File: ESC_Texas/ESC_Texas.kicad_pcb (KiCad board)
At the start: 4 copper layers, 118 x 72 mm, 149 parts, among them IC1 nRF52840-QFAA-F-R7, IC10 UCC21331CQDRQ1, IC11 LM3480IM3-3.3_NOPB, IC2 UCC21331CQDRQ1, IC3 AD8411AWBRZ, IC4 MC78L05ACHT1G, IC5 AD8411AWBRZ, IC6 MC78L05ACHT1G, IC7 UCC21331CQDRQ1, IC8 AD8411AWBRZ, IC9 MC78L05ACHT1G, J1 Conn_01x10_Pin, J10 Conn_01x03_Pin, J12 Conn_01x05_Pin, J13 Conn_01x06_Pin, J2 Conn_01x05_Pin, J3 Motor, J4 Conn_01x05_Pin, J5 Conn_01x03_Pin, J6 Conn_01x03_Pin, J7 Conn_01x03_Pin, J8 Conn_01x03_Pin, J9 Conn_01x03_Pin, Q1 IPD100N06S4, Q2 IPD100N06S4, Q3 IPD100N06S4, Q4 IPD100N06S4, Q5 IPD100N06S4, Q6 IPD100N06S4, Y1 CM7V-T1A-32.768kHz, Y2 32MHz

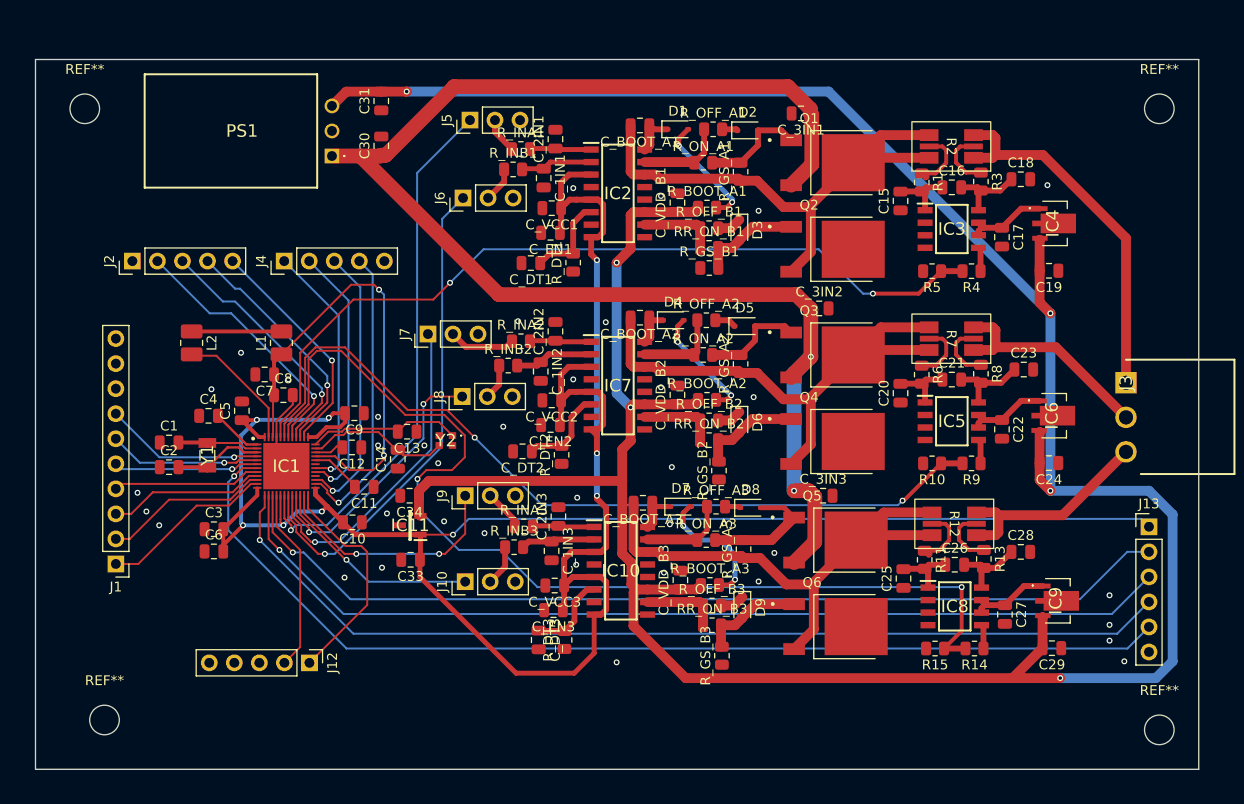
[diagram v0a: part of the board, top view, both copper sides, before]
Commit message: Removed excess pin headers
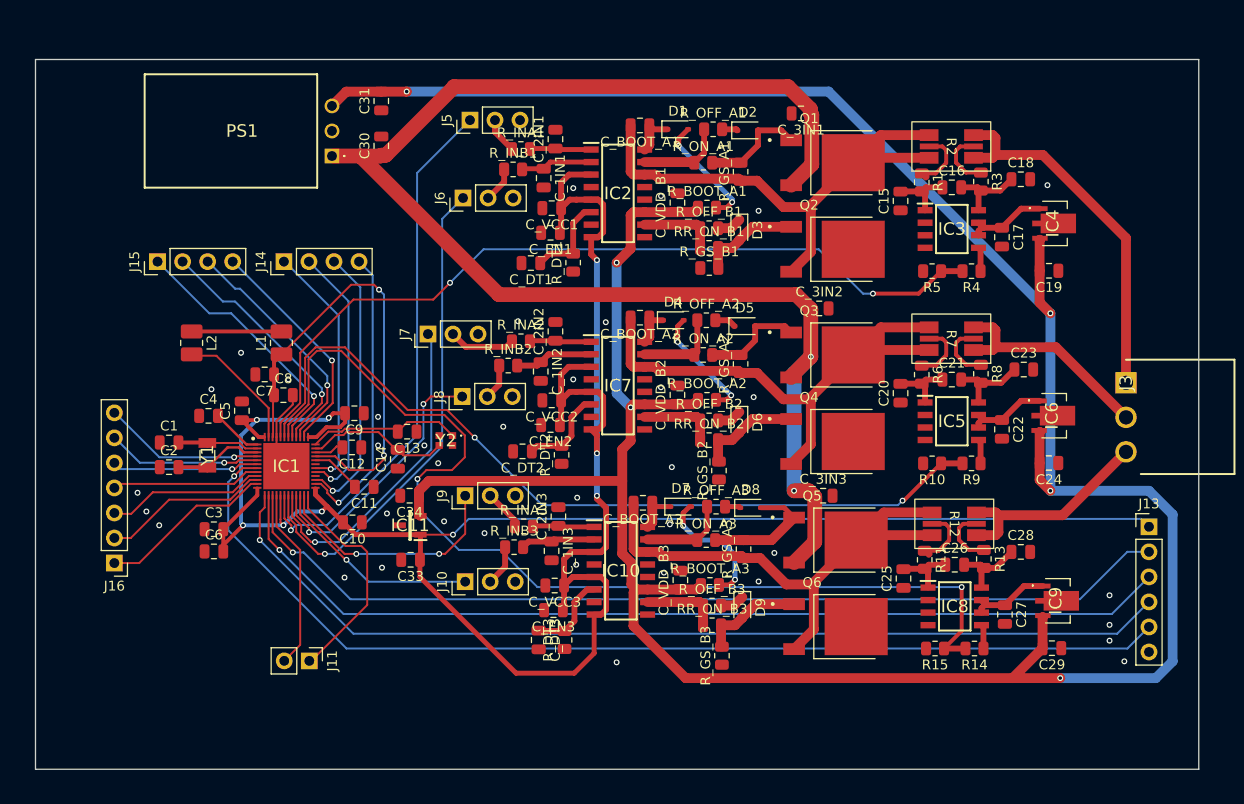
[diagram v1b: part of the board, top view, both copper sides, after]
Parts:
- removed J1: Conn_01x10_Pin, Connector_PinHeader_2.54mm:PinHeader_1x10_P2.54mm_Vertical
- removed J12, J2, J4: Conn_01x05_Pin, Connector_PinHeader_2.54mm:PinHeader_1x05_P2.54mm_Vertical
- removed REF** (x4): MountingHole_3mm, MountingHole:MountingHole_3mm
- added J11: Conn_01x02_Pin, Connector_PinHeader_2.54mm:PinHeader_1x02_P2.54mm_Vertical, F.Cu at (119.8, 135.0)
- added J14: Conn_01x04_Pin, Connector_PinHeader_2.54mm:PinHeader_1x04_P2.54mm_Vertical, F.Cu at (117.2, 94.5)
- added J15: Conn_01x04_Pin, Connector_PinHeader_2.54mm:PinHeader_1x04_P2.54mm_Vertical, F.Cu at (104.4, 94.5)
- added J16: Conn_01x07_Pin, Connector_PinHeader_2.54mm:PinHeader_1x07_P2.54mm_Vertical, F.Cu at (100.0, 125.1)
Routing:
- net P0.03: track 24.8 -> 24.3 mm

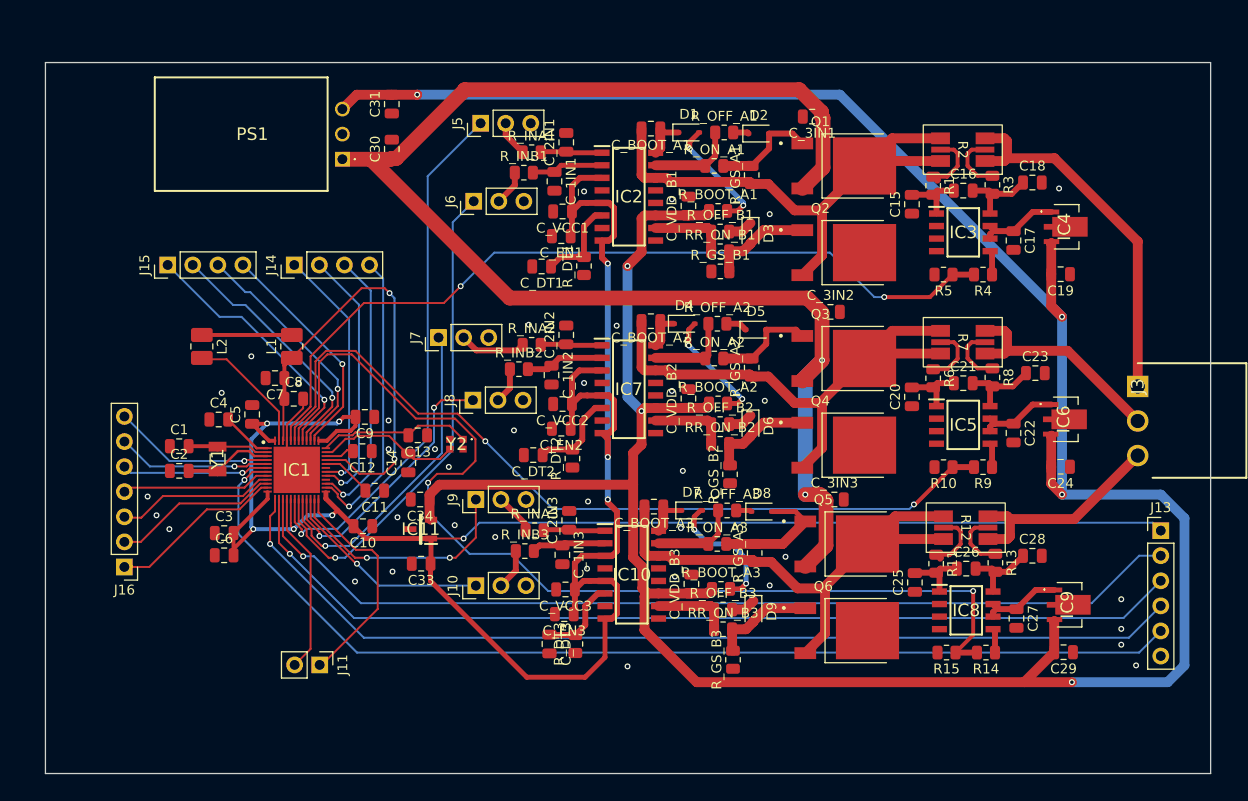
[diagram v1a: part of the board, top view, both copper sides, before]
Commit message: More gnd vias added
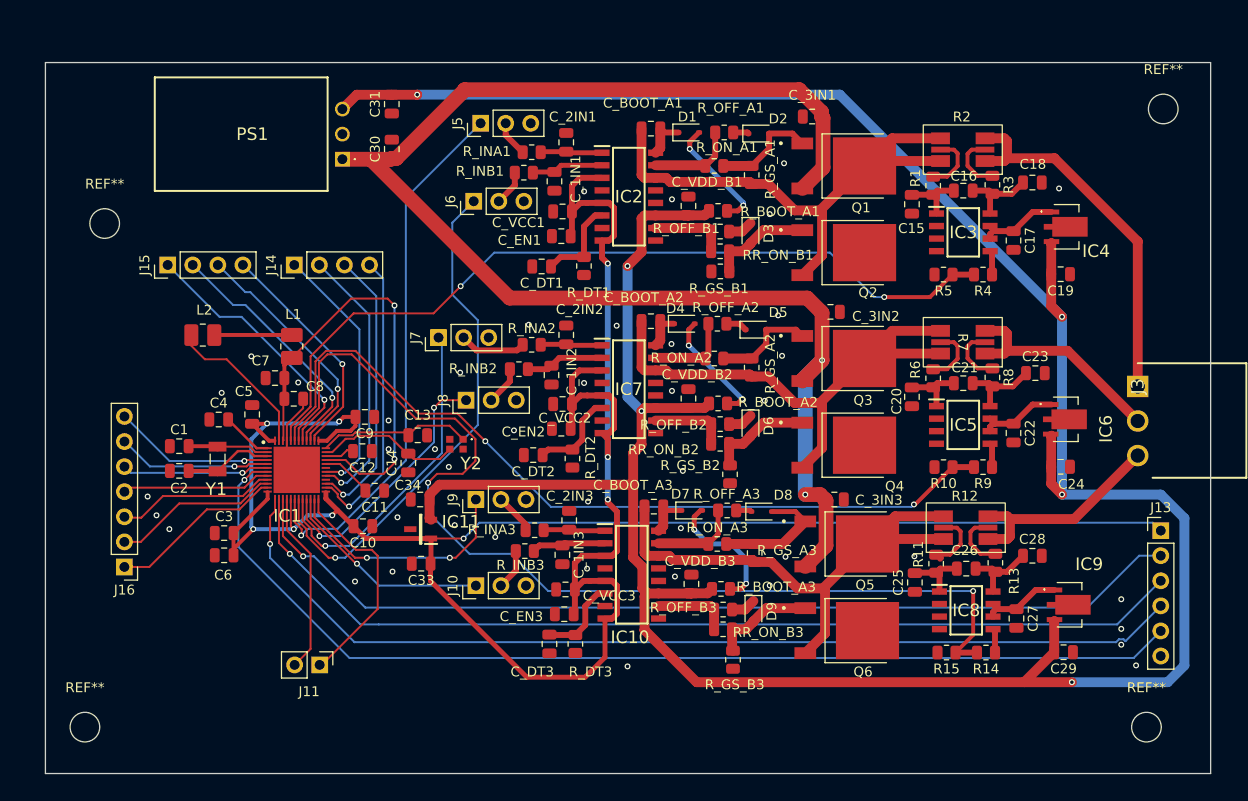
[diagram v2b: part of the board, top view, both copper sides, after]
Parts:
- added REF**: MountingHole_3mm, MountingHole:MountingHole_3mm, F.Cu at (98.0, 90.3)
- added REF**: MountingHole_3mm, MountingHole:MountingHole_3mm, F.Cu at (203.5, 141.3)
- added REF**: MountingHole_3mm, MountingHole:MountingHole_3mm, F.Cu at (205.2, 78.7)
- added REF**: MountingHole_3mm, MountingHole:MountingHole_3mm, F.Cu at (96.0, 141.3)
- moved L2 1.15 mm to (107.9, 101.6), turned to 180 degrees
- moved J8 0.69 mm to (134.6, 108.2)
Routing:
- net Net-(IC1-DCC): track 13.0 -> 15.7 mm
- net P0.20: track 50.4 -> 52.5 mm
- net P0.13: track 100.2 -> 101.6 mm
- net DEC6: track 47.2 -> 45.9 mm
- net Net-(L1-Pad2): track 9.11 -> 7.86 mm
- net P0.08: track 107.7 -> 108.9 mm
- net P0.09: track 26.7 -> 27.6 mm
- net P0.10: track 25.6 -> 26.4 mm
- net P0.22: track 27.6 -> 26.9 mm
- net GND: vias 37 -> 43

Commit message: Started new additions
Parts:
- removed REF** (x4): MountingHole_3mm, MountingHole:MountingHole_3mm
- moved C15 2.34 mm to (180.2, 90.7)
- moved Q2 1.60 mm to (171.3, 93.2)
- moved Q1 1.53 mm to (171.6, 83.6)
- moved C_3IN2 0.65 mm to (170.8, 99.2), turned to 180 degrees
- moved C_3IN1 0.65 mm to (169.2, 79.0)
- moved Q5 0.14 mm to (173.3, 122.8)
- moved Q3 0.11 mm to (172.8, 104.0)
- moved Q6 0.10 mm to (173.2, 131.6)
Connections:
- Q1 pad 2: /Phase1/Driver_subsheet_1/VSSA -> +36V
- Q1 pad 3: +36V -> /Phase1/Driver_subsheet_1/VSSA
- Q2 pad 2: GND -> /Phase1/Driver_subsheet_1/VSSA
- Q2 pad 3: /Phase1/Driver_subsheet_1/VSSA -> GND
- Q3 pad 2: /Phase2/Driver_subsheet_1/VSSA -> +36V
- Q3 pad 3: +36V -> /Phase2/Driver_subsheet_1/VSSA
- Q4 pad 2: GND -> /Phase2/Driver_subsheet_1/VSSA
- Q4 pad 3: /Phase2/Driver_subsheet_1/VSSA -> GND
- Q5 pad 2: /Phase3/Driver_subsheet_1/VSSA -> +36V
- Q5 pad 3: +36V -> /Phase3/Driver_subsheet_1/VSSA
- Q6 pad 2: GND -> /Phase3/Driver_subsheet_1/VSSA
- Q6 pad 3: /Phase3/Driver_subsheet_1/VSSA -> GND
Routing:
- net +36V: track 145.1 -> 63.4 mm, vias 2 -> 27
- net /Phase3/Driver_subsheet_1/VSSA: track 55.0 -> 18.5 mm
- net /Phase2/Driver_subsheet_1/VSSA: track 55.0 -> 32.2 mm
- net /Phase1/Driver_subsheet_1/VSSA: track 55.0 -> 38.7 mm
- net /Phase3/Driver_subsheet_1/GateA: track 12.7 -> 8.08 mm
- net /Phase2/Driver_subsheet_1/GateB: track 10.5 -> 6.62 mm
- net /Phase2/Driver_subsheet_1/GateA: track 10.3 -> 6.41 mm
- net /Phase3/Driver_subsheet_1/GateB: track 10.5 -> 7.16 mm
- net Net-(IC3--IN): track 6.48 -> 4.32 mm
- net /Phase1/Driver_subsheet_1/GateB: track 10.4 -> 8.74 mm
- net /Phase1/Driver_subsheet_1/GateA: track 10.7 -> 9.05 mm
- net P0.31: track 83.7 -> 84.6 mm
- net GND: vias 43 -> 44
- added copper zone on B.Cu, net +36V
- added copper zone on F.Cu, net +36V
- added copper zone on In2.Cu, net +36V
- added copper zone on F.Cu, net /Phase1/Driver_subsheet_1/VSSA

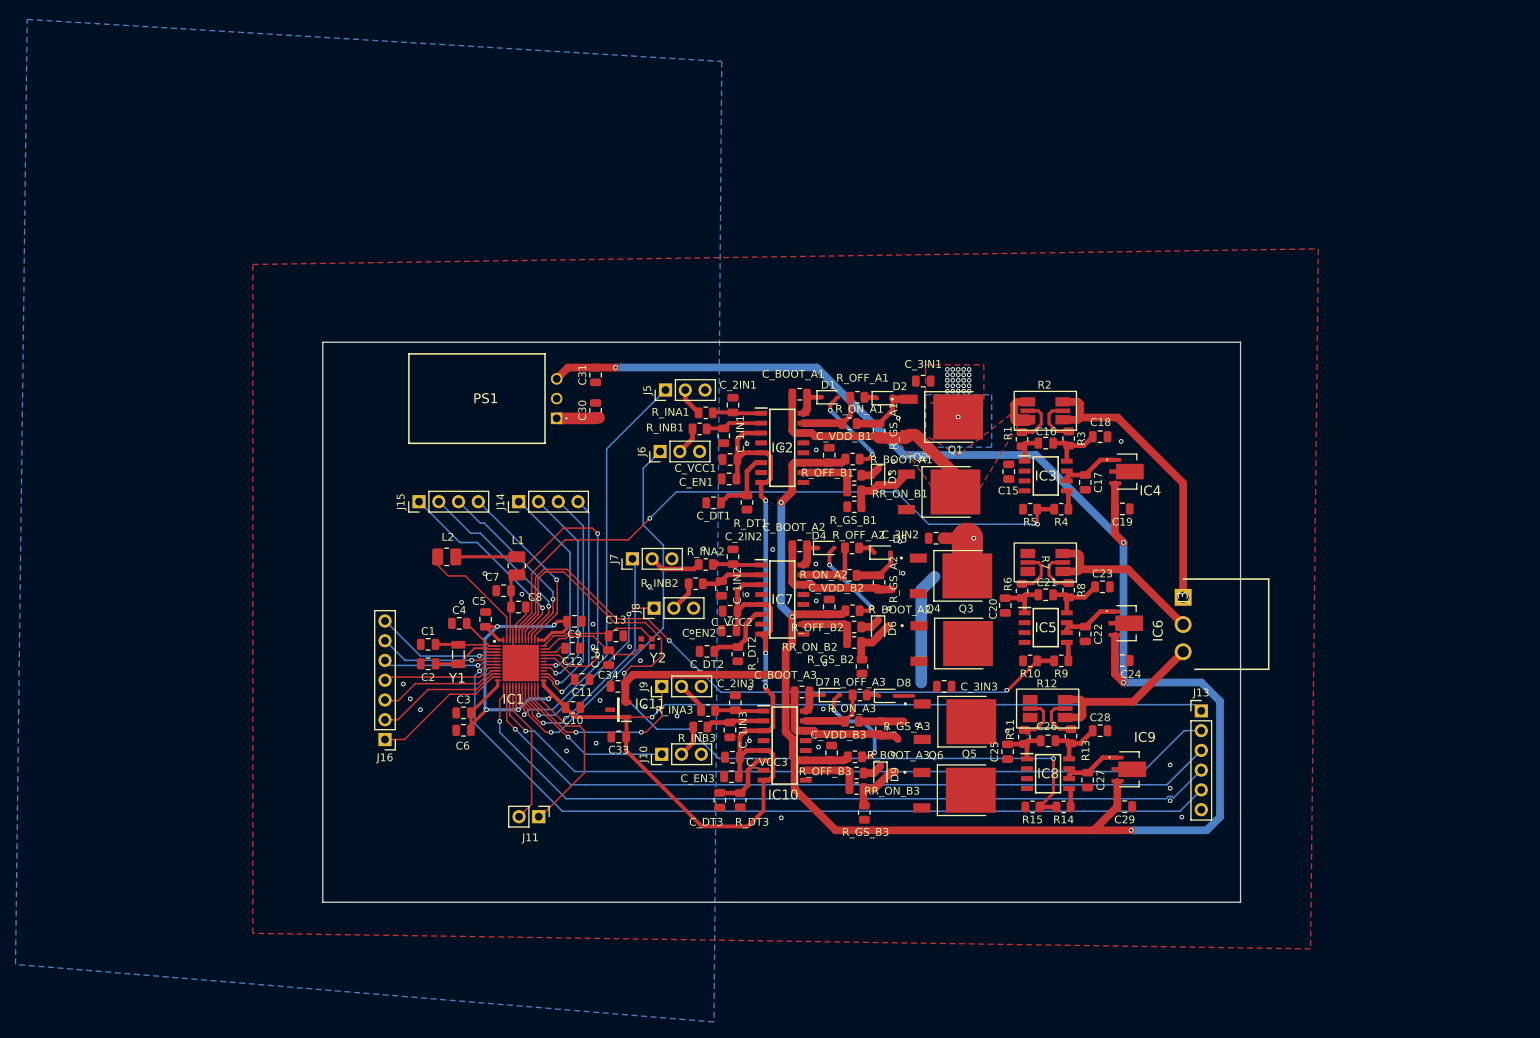
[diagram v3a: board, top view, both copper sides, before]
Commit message: Added capacitors and more
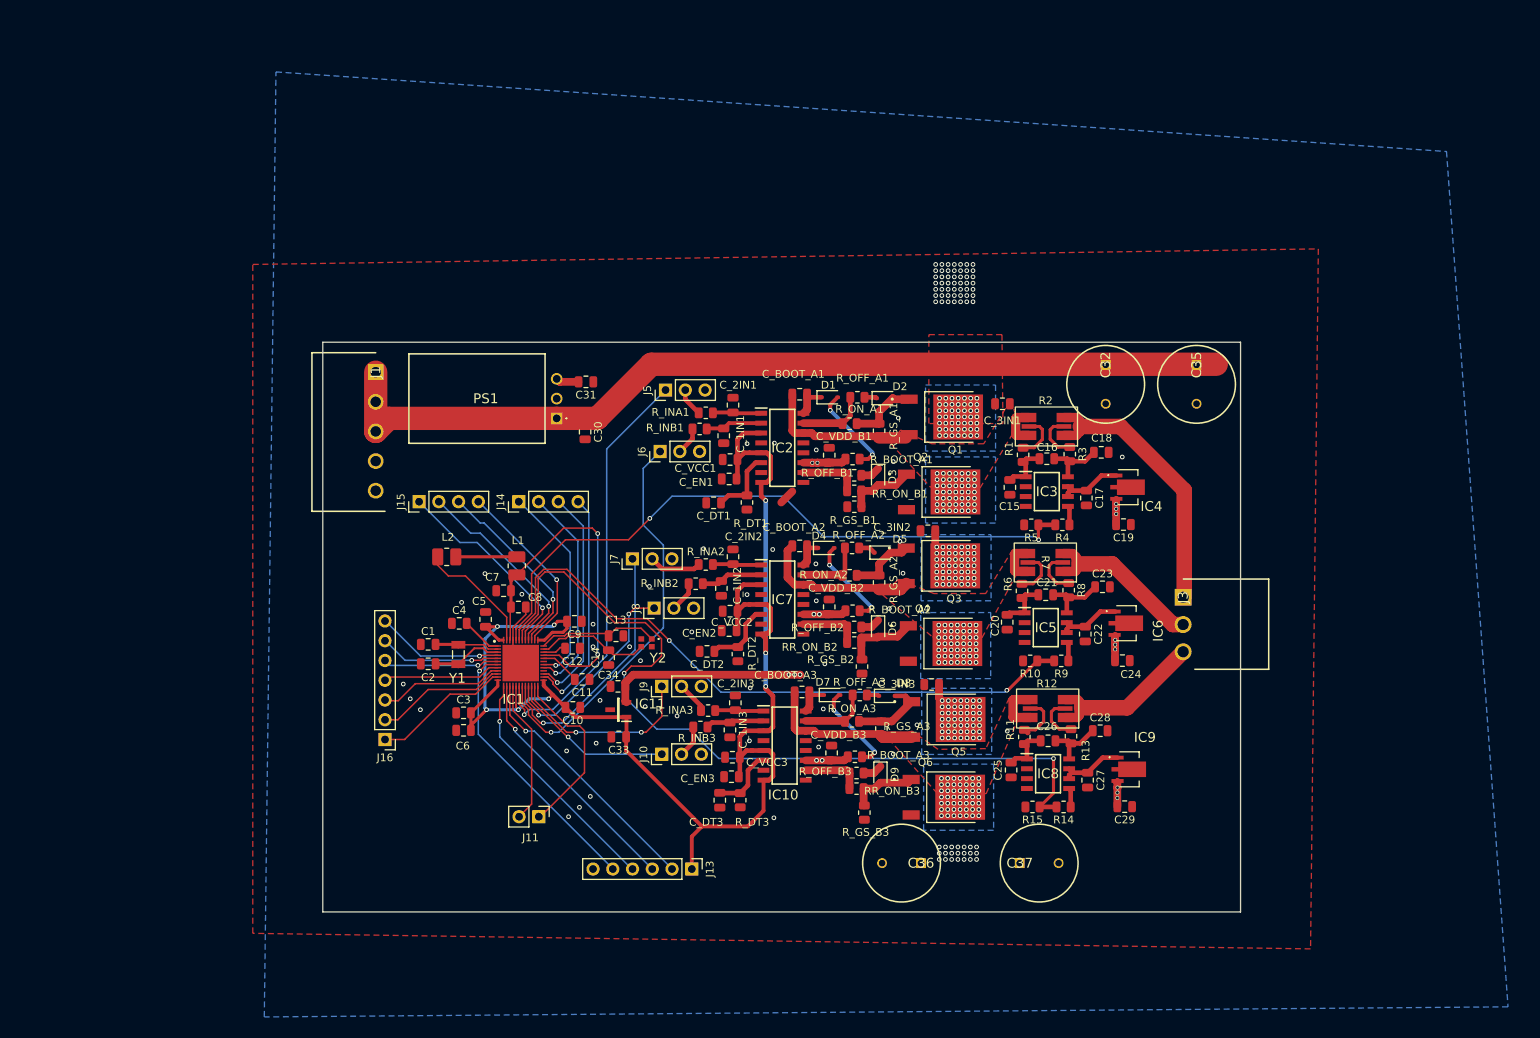
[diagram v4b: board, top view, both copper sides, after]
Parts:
- added C32: 270uF, A750MV277M1HAAE018:CAPPRD500W65D1000H1600, F.Cu at (192.7, 76.9)
- added C35: 270uF, A750MV277M1HAAE018:CAPPRD500W65D1000H1600, F.Cu at (204.3, 76.9)
- added C36: 270uF, A750MV277M1HAAE018:CAPPRD500W65D1000H1600, F.Cu at (168.9, 141.0)
- added C37: 270uF, A750MV277M1HAAE018:CAPPRD500W65D1000H1600, F.Cu at (181.6, 141.0)
- added J1: Battery, 691322310005:SHDRRA5W80P0X381_1X5_2024X920X720P, F.Cu at (98.8, 77.9)
- C_3IN1, C_3IN2, C_3IN3: value 33pF -> 1uF
- moved J13 68.6 mm to (139.4, 141.7), turned to -90 degrees
- moved C_3IN1 10.6 mm to (179.4, 81.9), turned to 0 degrees
- moved C30 3.08 mm to (125.7, 85.5), turned to -90 degrees
- moved C25 2.39 mm to (180.5, 129.0)
- moved C20 2.16 mm to (180.0, 110.0)
- moved Q3 2.02 mm to (171.2, 102.8)
- moved C16 2.01 mm to (185.1, 89.0)
- moved IC3 2.01 mm to (185.1, 93.2)
- moved R4 2.01 mm to (187.1, 97.5)
- moved R5 2.01 mm to (183.1, 97.5)
- moved C17 2.01 mm to (190.2, 94.0)
- moved C19 2.01 mm to (194.9, 97.4)
- moved IC4 2.01 mm to (194.3, 92.6)
- moved R1 2.01 mm to (182.0, 88.5)
- moved C15 2.01 mm to (180.3, 92.7)
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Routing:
- net +15V: track 298.6 -> 132.5 mm, vias 6 -> 18
- net +36V: track 63.4 -> 225.4 mm, vias 27 -> 217
- net P0.08: track 108.9 -> 35.4 mm
- net P0.13: track 101.6 -> 30.9 mm
- net VDD: track 261.8 -> 193.0 mm, vias 9 -> 8
- net P0.14: track 99.0 -> 31.3 mm
- net P0.17: track 97.8 -> 32.8 mm
- net /Phase1/Driver_subsheet_1/VSSA: track 38.7 -> 26.2 mm, vias 0 -> 49
- net /Phase3/Driver_subsheet_1/VSSA: track 18.5 -> 26.8 mm, vias 0 -> 49
- net /Phase2/Driver_subsheet_1/VSSA: track 32.2 -> 26.1 mm, vias 0 -> 49
- net /Phase2/Driver_subsheet_1/GateB: track 6.62 -> 9.53 mm
- net /Phase2/Driver_subsheet_1/GateA: track 6.41 -> 8.67 mm
- net Net-(IC3--IN): track 4.32 -> 6.56 mm
- net /Phase3/Driver_subsheet_1/GateA: track 8.08 -> 10.2 mm
- net /Phase3/Driver_subsheet_1/GateB: track 7.16 -> 8.80 mm
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- added copper zone on In2.Cu, net +15V
- added copper zone on B.Cu, net /Phase1/Driver_subsheet_1/VSSA
- added copper zone on B.Cu, net /Phase2/Driver_subsheet_1/VSSA
- added copper zone on F.Cu, net /Phase2/Driver_subsheet_1/VSSA
- added copper zone on B.Cu, net /Phase3/Driver_subsheet_1/VSSA
- added copper zone on F.Cu, net /Phase3/Driver_subsheet_1/VSSA
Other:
- board size 118 x 72 mm -> 118 x 73.2 mm

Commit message: Fixed like 100 errors
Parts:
- added J2: Conn_01x08_Pin, Connector_PinHeader_2.54mm:PinHeader_1x08_P2.54mm_Vertical, F.Cu at (101.3, 139.6)
- moved J1 6.13 mm to (98.9, 84.0)
- moved C32 1.38 mm to (194.0, 76.6)
- moved C35 1.26 mm to (205.6, 76.9)
- moved C36 0.82 mm to (169.2, 140.2)
- moved C37 0.66 mm to (181.8, 141.6)
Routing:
- net P0.29: track 107.1 -> 108.1 mm
- net +15V: track 132.5 -> 133.6 mm, vias 18 -> 15
- net +36V: track 225.4 -> 224.7 mm, vias 217 -> 189
- net GND: vias 43 -> 105
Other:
- board text added: "GND"
